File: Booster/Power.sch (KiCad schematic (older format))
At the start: 6 parts

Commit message: Over current protection and detection - with detection delay and release delay.
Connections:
- net labels added: +15V
- net labels removed: +12V
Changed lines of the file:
@@
-$EndComp
-$Comp
-L +12V #PWR?
-U 1 1 59E902FB
-P 5350 3000
-F 0 "#PWR?" H 5350 2850 50  0001 C CNN
-F 1 "+12V" H 5350 3140 50  0000 C CNN
-F 2 "" H 5350 3000 50  0001 C CNN
-F 3 "" H 5350 3000 50  0001 C CNN
-	1    5350 3000
-	1    0    0    -1
 $EndComp
 $Comp
@@
 Wire Wire Line
 	3850 3500 3850 4100
+$Comp
+L +15V #PWR?
+U 1 1 5A093AB5
+P 5350 3000
+F 0 "#PWR?" H 5350 2850 50  0001 C CNN
+F 1 "+15V" H 5350 3140 50  0000 C CNN
+F 2 "" H 5350 3000 50  0000 C CNN
+F 3 "" H 5350 3000 50  0000 C CNN
+	1    5350 3000
+	1    0    0    -1
+$EndComp
 $EndSCHEMATC

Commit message: Getting close to feature complete for a single channel.
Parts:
- added D?: min 20V 3A, symbol D
- J?: value 12VDC -> 16VDC
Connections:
- net +15V: now also D?.1 (K); no longer J?.2 (Pin_2)
- new net: D?.2 (A), J?.2 (Pin_2)
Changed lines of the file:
@@
 P 3200 3500
 F 0 "J?" H 3200 3600 50  0000 C CNN
-F 1 "12VDC" H 3200 3300 50  0000 C CNN
+F 1 "16VDC" H 3200 3300 50  0000 C CNN
 F 2 "" H 3200 3500 50  0001 C CNN
 F 3 "" H 3200 3500 50  0001 C CNN
@@
 $EndComp
 Wire Wire Line
-	8250 3400 8250 3050
-Wire Wire Line
-	6650 3650 6650 3400
+	6650 3400 6650 3650
 Wire Wire Line
 	7150 4100 7150 3700
@@
 Connection ~ 6650 4100
 Wire Wire Line
-	3400 3500 3850 3500
+	3400 3500 3500 3500
 Wire Wire Line
 	7600 4100 7600 3950
@@
 Connection ~ 7150 4100
 Wire Wire Line
-	3850 4100 7600 4100
+	3500 4100 7600 4100
 Wire Wire Line
 	6650 4100 6650 3950
 Connection ~ 6650 3400
 Wire Wire Line
-	3400 3400 6850 3400
+	3950 3400 6850 3400
 Wire Wire Line
 	7450 3400 8250 3400
@@
 Connection ~ 5350 4100
 Wire Wire Line
-	3850 3500 3850 4100
+	3500 3500 3500 4100
 $Comp
 L +15V #PWR?
@@
 	1    0    0    -1
 $EndComp
+Wire Wire Line
+	8250 3400 8250 3050
+$Comp
+L D D?
+U 1 1 5A0E87C4
+P 3800 3400
+F 0 "D?" H 3800 3500 50  0000 C CNN
+F 1 "min 20V 3A" H 3800 3300 50  0000 C CNN
+F 2 "" H 3800 3400 50  0001 C CNN
+F 3 "" H 3800 3400 50  0001 C CNN
+	1    3800 3400
+	-1   0    0    1
+$EndComp
+Wire Wire Line
+	3400 3400 3650 3400
 $EndSCHEMATC

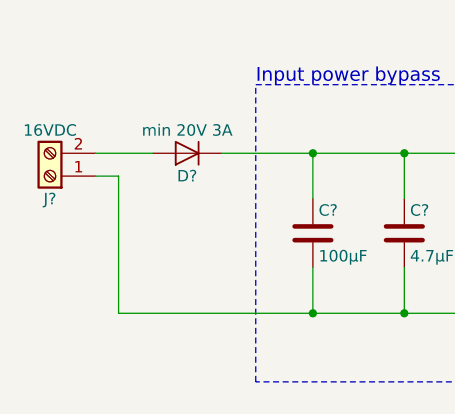
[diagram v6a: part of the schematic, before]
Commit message: Added meassurement tabs and other general "finalizing touches"
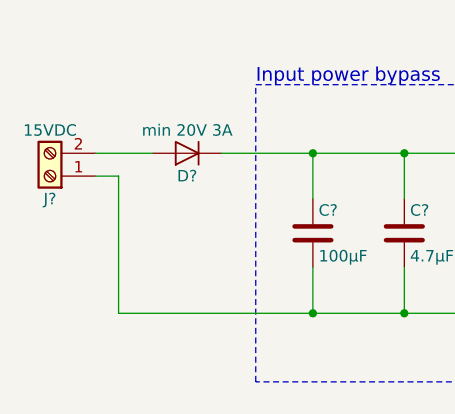
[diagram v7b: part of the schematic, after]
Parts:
- J?: value 16VDC -> 15VDC
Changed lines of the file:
@@
 P 3200 3500
 F 0 "J?" H 3200 3600 50  0000 C CNN
-F 1 "16VDC" H 3200 3300 50  0000 C CNN
+F 1 "15VDC" H 3200 3300 50  0000 C CNN
 F 2 "" H 3200 3500 50  0001 C CNN
 F 3 "" H 3200 3500 50  0001 C CNN

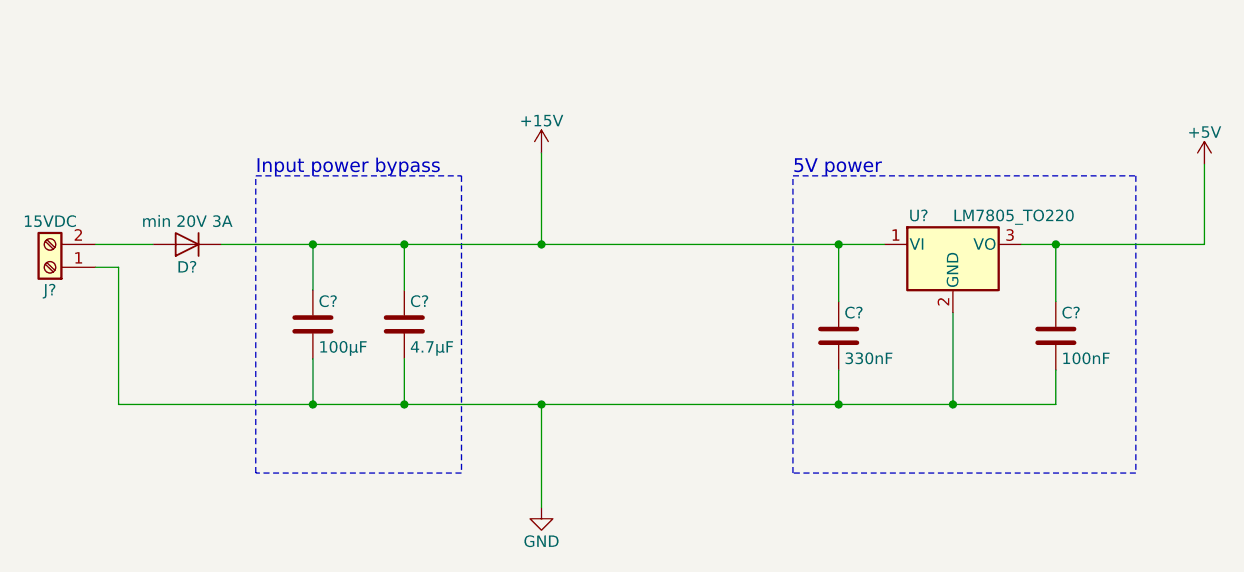
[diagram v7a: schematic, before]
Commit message: Fixed missing connections.
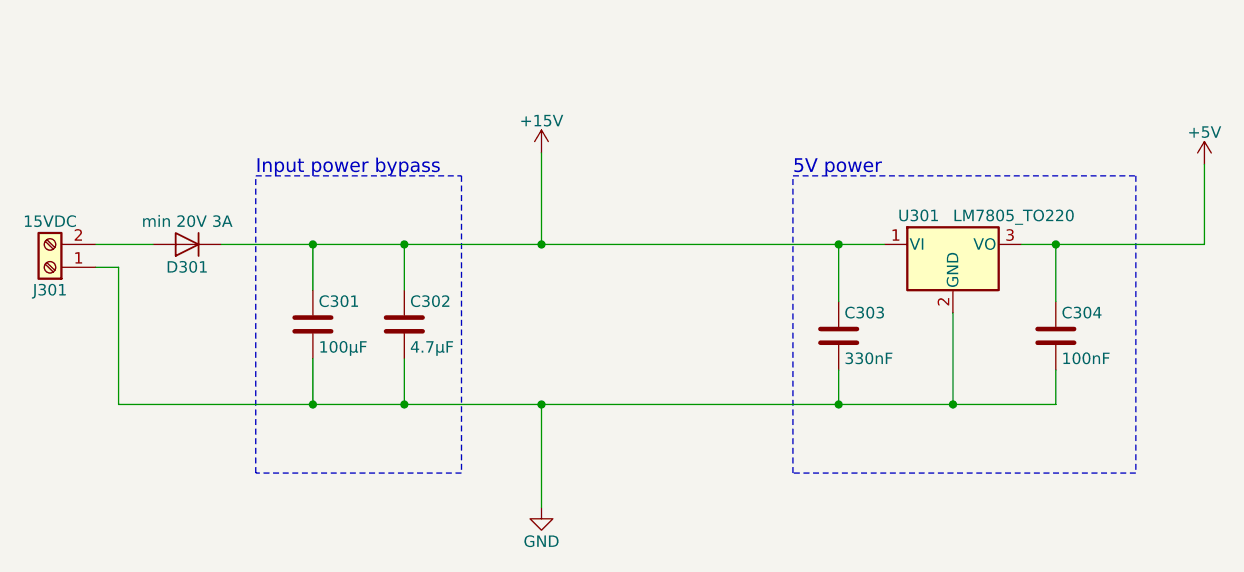
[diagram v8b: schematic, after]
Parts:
- gave numbers to parts that had none: 7
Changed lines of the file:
@@
 $EndDescr
 $Comp
-L LM7805_TO220 U?
+L LM7805_TO220 U301
 U 1 1 59E902F4
 P 7150 3400
-F 0 "U?" H 7000 3525 50  0000 C CNN
+F 0 "U301" H 7000 3525 50  0000 C CNN
 F 1 "LM7805_TO220" H 7150 3525 50  0000 L CNN
 F 2 "TO_SOT_Packages_THT:TO-220_Vertical" H 7150 3625 50  0001 C CIN
@@
 $EndComp
 $Comp
-L C C?
+L C C303
 U 1 1 59E90304
 P 6650 3800
-F 0 "C?" H 6675 3900 50  0000 L CNN
+F 0 "C303" H 6675 3900 50  0000 L CNN
 F 1 "330nF" H 6675 3700 50  0000 L CNN
 F 2 "" H 6688 3650 50  0001 C CNN
@@
 $EndComp
 $Comp
-L C C?
+L C C304
 U 1 1 59E9030C
 P 7600 3800
-F 0 "C?" H 7625 3900 50  0000 L CNN
+F 0 "C304" H 7625 3900 50  0000 L CNN
 F 1 "100nF" H 7625 3700 50  0000 L CNN
 F 2 "" H 7638 3650 50  0001 C CNN
@@
 $EndComp
 $Comp
-L GND #PWR?
+L GND #PWR08
 U 1 1 59E90316
 P 5350 4550
-F 0 "#PWR?" H 5350 4300 50  0001 C CNN
+F 0 "#PWR08" H 5350 4300 50  0001 C CNN
 F 1 "GND" H 5350 4400 50  0000 C CNN
 F 2 "" H 5350 4550 50  0001 C CNN
@@
 $EndComp
 $Comp
-L Screw_Terminal_01x02 J?
+L Screw_Terminal_01x02 J301
 U 1 1 59E9033D
 P 3200 3500
-F 0 "J?" H 3200 3600 50  0000 C CNN
+F 0 "J301" H 3200 3600 50  0000 C CNN
 F 1 "15VDC" H 3200 3300 50  0000 C CNN
 F 2 "" H 3200 3500 50  0001 C CNN
@@
 $EndComp
 $Comp
-L C C?
+L C C301
 U 1 1 59E90526
 P 4350 3750
-F 0 "C?" H 4375 3850 50  0000 L CNN
+F 0 "C301" H 4375 3850 50  0000 L CNN
 F 1 "100µF" H 4375 3650 50  0000 L CNN
 F 2 "" H 4388 3600 50  0001 C CNN
@@
 $EndComp
 $Comp
-L C C?
+L C C302
 U 1 1 59E905AF
 P 4750 3750
-F 0 "C?" H 4775 3850 50  0000 L CNN
+F 0 "C302" H 4775 3850 50  0000 L CNN
 F 1 "4.7µF" H 4775 3650 50  0000 L CNN
 F 2 "" H 4788 3600 50  0001 C CNN
@@
 	7450 3400 8250 3400
 $Comp
-L +5V #PWR?
+L +5V #PWR09
 U 1 1 59E9089F
 P 8250 3050
-F 0 "#PWR?" H 8250 2900 50  0001 C CNN
+F 0 "#PWR09" H 8250 2900 50  0001 C CNN
 F 1 "+5V" H 8250 3190 50  0000 C CNN
 F 2 "" H 8250 3050 50  0001 C CNN
@@
 	3500 3500 3500 4100
 $Comp
-L +15V #PWR?
+L +15V #PWR010
 U 1 1 5A093AB5
 P 5350 3000
-F 0 "#PWR?" H 5350 2850 50  0001 C CNN
+F 0 "#PWR010" H 5350 2850 50  0001 C CNN
 F 1 "+15V" H 5350 3140 50  0000 C CNN
 F 2 "" H 5350 3000 50  0000 C CNN
@@
 	8250 3400 8250 3050
 $Comp
-L D D?
+L D D301
 U 1 1 5A0E87C4
 P 3800 3400
-F 0 "D?" H 3800 3500 50  0000 C CNN
+F 0 "D301" H 3800 3500 50  0000 C CNN
 F 1 "min 20V 3A" H 3800 3300 50  0000 C CNN
 F 2 "" H 3800 3400 50  0001 C CNN
